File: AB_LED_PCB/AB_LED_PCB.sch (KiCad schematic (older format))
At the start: 15 parts, among them J1 Conn_01x03_Male

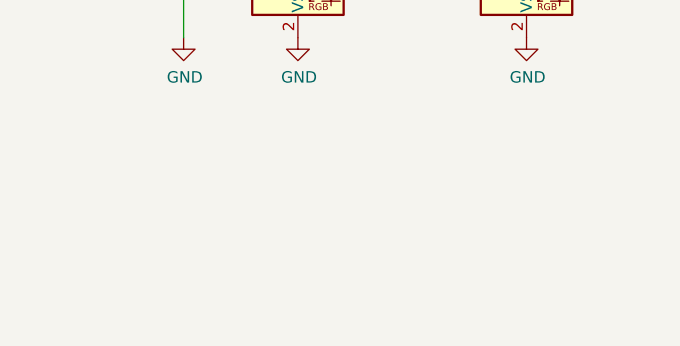
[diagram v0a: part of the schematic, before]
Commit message: added logo and routing
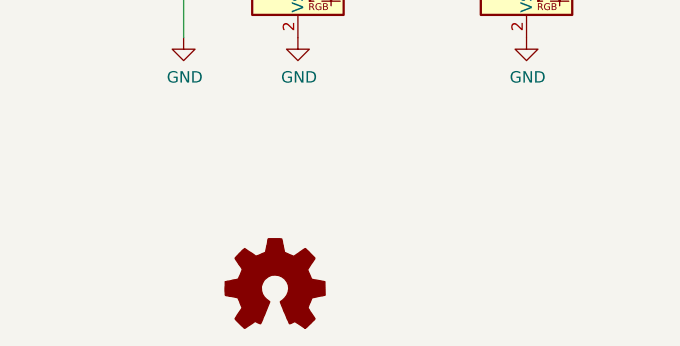
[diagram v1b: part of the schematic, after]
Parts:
- added SYM1: Logo_Open_Hardware_Small, Symbol:OSHW-Logo2_7.3x6mm_SilkScreen, symbol Graphic:Logo_Open_Hardware_Small
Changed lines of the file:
@@
 	2500 4000 2250 4000
 NoConn ~ 9300 4100
+$Comp
+L Graphic:Logo_Open_Hardware_Small SYM1
+U 1 1 607341E2
+P 2900 5500
+F 0 "SYM1" H 2900 5775 50  0001 C CNN
+F 1 "Logo_Open_Hardware_Small" H 2900 5275 50  0001 C CNN
+F 2 "Symbol:OSHW-Logo2_7.3x6mm_SilkScreen" H 2900 5500 50  0001 C CNN
+F 3 "~" H 2900 5500 50  0001 C CNN
+	1    2900 5500
+	1    0    0    -1
+$EndComp
 $EndSCHEMATC
